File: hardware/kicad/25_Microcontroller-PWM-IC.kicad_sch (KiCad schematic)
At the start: 16 parts, among them U78 PCA9685PW,118

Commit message: starting erc check
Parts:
- C117, C118: footprint Capacitor_SMD:C_0603_1608Metric -> 5v rail sm-easyedapro:C0603
- R170, R171, R176, R177, R178, R179, R180: footprint Resistor_SMD:R_0603_1608Metric -> 5v rail sm-easyedapro:R0603
- R181, R182, R183, R184, R186, R188: footprint Resistor_SMD:R_0402_1005Metric -> 5v rail sm-easyedapro:R0402; LCSC Part Name 厚膜电阻 10kΩ ±1% 50mW -> 10kΩ ±1% 62.5mW 厚膜电阻; Manufacturer YAGEO(国巨) -> UNI-ROYAL(厚声); Manufacturer Part RC0201FR-0710KL -> 0402WGF1002TCE; Supplier Part C106225 -> C25744
- U78: footprint Package_SO:TSSOP-28_4.4x9.7mm_P0.65mm -> 5v rail sm-easyedapro:TSSOP-28_L9.7-W4.4-P0.65-LS6.4-TL

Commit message: added protection to servo pins
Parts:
- removed R170, R171, R176, R177, R178, R179, R180: 47Ω, 5v rail sm-easyedapro:R0603, symbol 5v rail sm-easyedapro:RS-03K47R0FT
- added U3201: EXB2HV102JV, JLCImport:EXB2HV102JV, symbol JLCImport:EXB2HV102JV
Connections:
- net OUT0: now also U3201.1
- net OUT1: now also U3201.2
- net OUT2: now also U3201.3
- net OUT3: now also U3201.4
- net OUT4: now also U3201.5
- net OUT5: now also U3201.6
- net OUT6: now also U3201.7
- net at U78.6 (LED0): now also U3201.16
- net at U78.10 (LED4): now also U3201.12
- net at U78.7 (LED1): now also U3201.15
- net at U78.8 (LED2): now also U3201.14
- net at U78.9 (LED3): now also U3201.13
- net at U78.12 (LED6): now also U3201.10
- net at U78.11 (LED5): now also U3201.11

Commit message: Update KiCad footprints and schematic placements
Convert and normalize multiple KiCad footprints and adjust schematic symbol placements. Upgraded EasyEDA and JLCImport footprints to modern pcbnew/footprint format (updated fp_line/pad primitives, uuids, embedded fonts/models), adjusted 3D model offsets, and expanded pad metadata. In schematics: moved EXB2HV102JV symbol position and added mirror Y, removed fields_autoplaced, set instance project path for U3201, and updated ServoConnectors port2 label to "sbus 3V". Also refreshed various PCB fp element UUIDs in svea_powerboard_rev3.kicad_pcb.
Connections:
- net OUT0: now also U3201.16; no longer U3201.1
- net OUT1: now also U3201.15; no longer U3201.2
- net OUT2: now also U3201.14; no longer U3201.3
- net OUT3: now also U3201.13; no longer U3201.4
- net OUT4: now also U3201.12; no longer U3201.5
- net OUT5: now also U3201.11; no longer U3201.6
- net OUT6: now also U3201.10; no longer U3201.7
- net at U78.12 (LED6): now also U3201.7; no longer U3201.10
- net at U78.11 (LED5): now also U3201.6; no longer U3201.11
- net at U78.10 (LED4): now also U3201.5; no longer U3201.12
- net at U78.9 (LED3): now also U3201.4; no longer U3201.13
- net at U78.8 (LED2): now also U3201.3; no longer U3201.14
- net at U78.7 (LED1): now also U3201.2; no longer U3201.15
- net at U78.6 (LED0): now also U3201.1; no longer U3201.16
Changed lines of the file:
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@@
 	(symbol
 		(lib_id "JLCImport:EXB2HV102JV")
-		(at 129.54 115.57 0)
+		(at 127 115.57 0)
+		(mirror y)
 		(unit 1)
 		(exclude_from_sim no)
@@
 		(on_board yes)
 		(dnp no)
-		(fields_autoplaced yes)
 		(property "Reference" "U3201"
 			(at 128.27 100.33 0)
@@
 		)
 		(property "Footprint" "JLCImport:EXB2HV102JV"
-			(at 129.54 115.57 0)
+			(at 127 115.57 0)
 			(effects
 				(font
@@
 		)
 		(property "Datasheet" "https://wmsc.lcsc.com/wmsc/upload/file/pdf/v2/lcsc/2011031536_PANASONIC-EXB2HV102JV_C713453.pdf"
-			(at 129.54 115.57 0)
+			(at 127 115.57 0)
 			(effects
 				(font
@@
 		)
 		(property "Description" "16 1kΩ 63mW 8 ±200ppm/℃ ±5% SMD-16P,3.8x1.6mm Resistor Networks, Arrays ROHS"
-			(at 129.54 115.57 0)
+			(at 127 115.57 0)
 			(effects
 				(font
@@
 		)
 		(property "LCSC" "C713453"
-			(at 129.54 115.57 0)
+			(at 127 115.57 0)
 			(effects
 				(font
@@
 		)
 		(property "Manufacturer" "PANASONIC"
-			(at 129.54 115.57 0)
+			(at 127 115.57 0)
 			(effects
 				(font
@@
 		)
 		(property "Manufacturer Part" "EXB2HV102JV"
-			(at 129.54 115.57 0)
+			(at 127 115.57 0)
 			(effects
 				(font
@@
 		)
 		(instances
-			(project ""
+			(project "svea_powerboard_rev3"
 				(path "/3f85abf4-0b95-4c4a-b7e9-06f59ca1ea3d/5c2e021f-c2d4-49e2-8c36-9a64f1f12001/8281c4bd-f2fa-451b-b37c-f7eda375ddce"
 					(reference "U3201")

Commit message: updating symbols to use kicad footprints where possible
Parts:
- C117, C118: footprint 5v rail sm-easyedapro:C0603 -> Capacitor_SMD:C_0603_1608Metric
- R181, R182, R183, R184, R186, R188: footprint 5v rail sm-easyedapro:R0402 -> Resistor_SMD:R_0402_1005Metric
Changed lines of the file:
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@@
 			)
 		)
-		(property "Footprint" "5v rail sm-easyedapro:R0402"
+		(property "Footprint" "Resistor_SMD:R_0402_1005Metric"
 			(at 130.81 72.39 0)
 			(effects
@@
 			)
 		)
-		(property "Footprint" "5v rail sm-easyedapro:R0402"
+		(property "Footprint" "Resistor_SMD:R_0402_1005Metric"
 			(at 196.85 107.95 0)
 			(effects
@@
 			)
 		)
-		(property "Footprint" "5v rail sm-easyedapro:C0603"
+		(property "Footprint" "Capacitor_SMD:C_0603_1608Metric"
 			(at 251.46 74.93 0)
 			(effects
@@
 			)
 		)
-		(property "Footprint" "5v rail sm-easyedapro:R0402"
+		(property "Footprint" "Resistor_SMD:R_0402_1005Metric"
 			(at 166.37 64.77 0)
 			(effects
@@
 			)
 		)
-		(property "Footprint" "5v rail sm-easyedapro:R0402"
+		(property "Footprint" "Resistor_SMD:R_0402_1005Metric"
 			(at 130.81 87.63 0)
 			(effects
@@
 			)
 		)
-		(property "Footprint" "5v rail sm-easyedapro:R0402"
+		(property "Footprint" "Resistor_SMD:R_0402_1005Metric"
 			(at 130.81 64.77 0)
 			(effects
@@
 			)
 		)
-		(property "Footprint" "5v rail sm-easyedapro:C0603"
+		(property "Footprint" "Capacitor_SMD:C_0603_1608Metric"
 			(at 236.22 74.93 0)
 			(effects
@@
 			)
 		)
-		(property "Footprint" "5v rail sm-easyedapro:R0402"
+		(property "Footprint" "Resistor_SMD:R_0402_1005Metric"
 			(at 130.81 80.01 0)
 			(effects

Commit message: updated more footprints
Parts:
- U78: footprint 5v rail sm-easyedapro:TSSOP-28_L9.7-W4.4-P0.65-LS6.4-TL -> Package_SO:TSSOP-28_4.4x9.7mm_P0.65mm
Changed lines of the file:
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@@
 			)
 		)
-		(property "Footprint" "5v rail sm-easyedapro:TSSOP-28_L9.7-W4.4-P0.65-LS6.4-TL"
+		(property "Footprint" "Package_SO:TSSOP-28_4.4x9.7mm_P0.65mm"
 			(at 171.45 111.76 0)
 			(effects

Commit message: various erc fixes
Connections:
- no-connect marks 0 -> 11
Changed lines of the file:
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@@
 		(color 0 0 0 0)
+	)
+	(no_connect
+		(at 184.15 115.57)
+	)
+	(no_connect
+		(at 184.15 118.11)
+	)
+	(no_connect
+		(at 184.15 110.49)
+	)
+	(no_connect
+		(at 184.15 123.19)
+	)
+	(no_connect
+		(at 184.15 128.27)
+	)
+	(no_connect
+		(at 184.15 125.73)
+	)
+	(no_connect
+		(at 120.65 125.73)
+	)
+	(no_connect
+		(at 184.15 120.65)
+	)
+	(no_connect
+		(at 135.89 125.73)
+	)
+	(no_connect
+		(at 184.15 113.03)
+	)
+	(no_connect
+		(at 158.75 125.73)
 	)
 	(wire

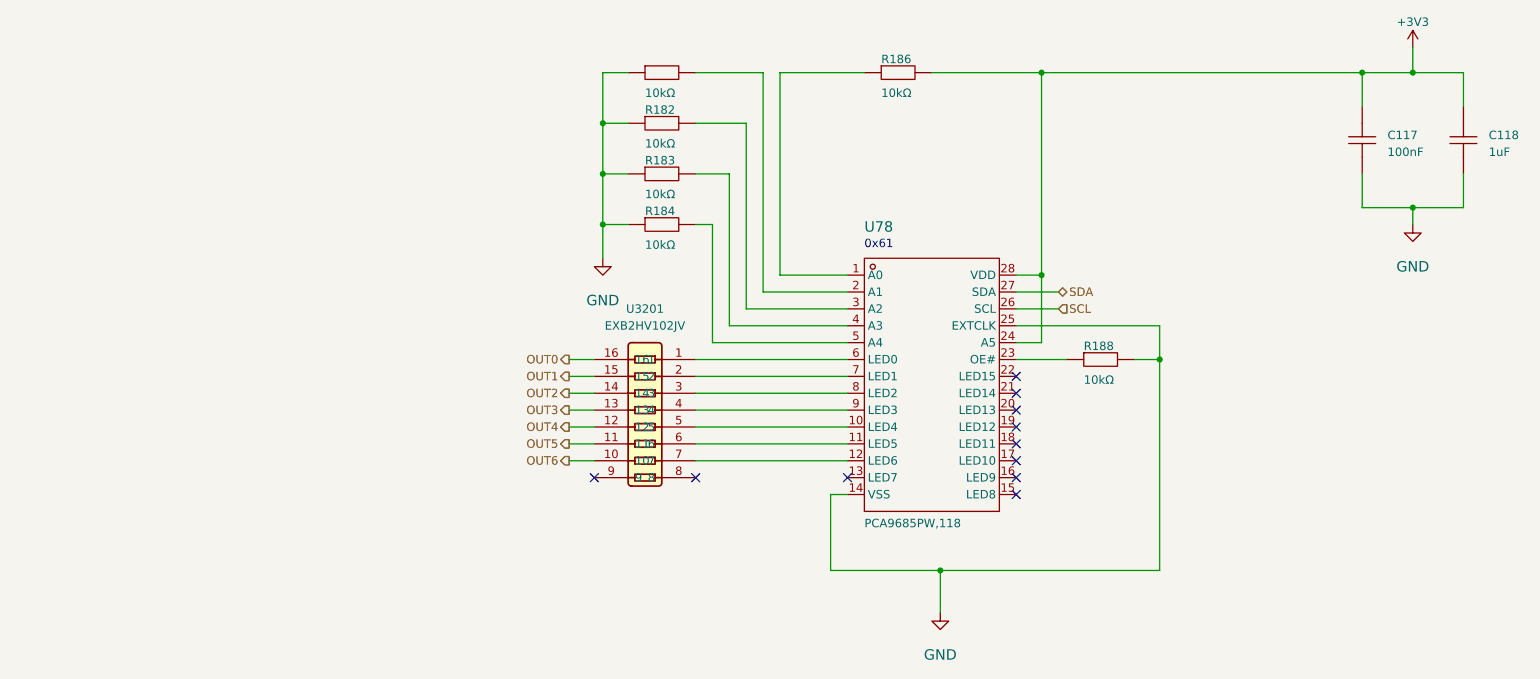
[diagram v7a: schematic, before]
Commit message: fixing inconsistencies in value convention
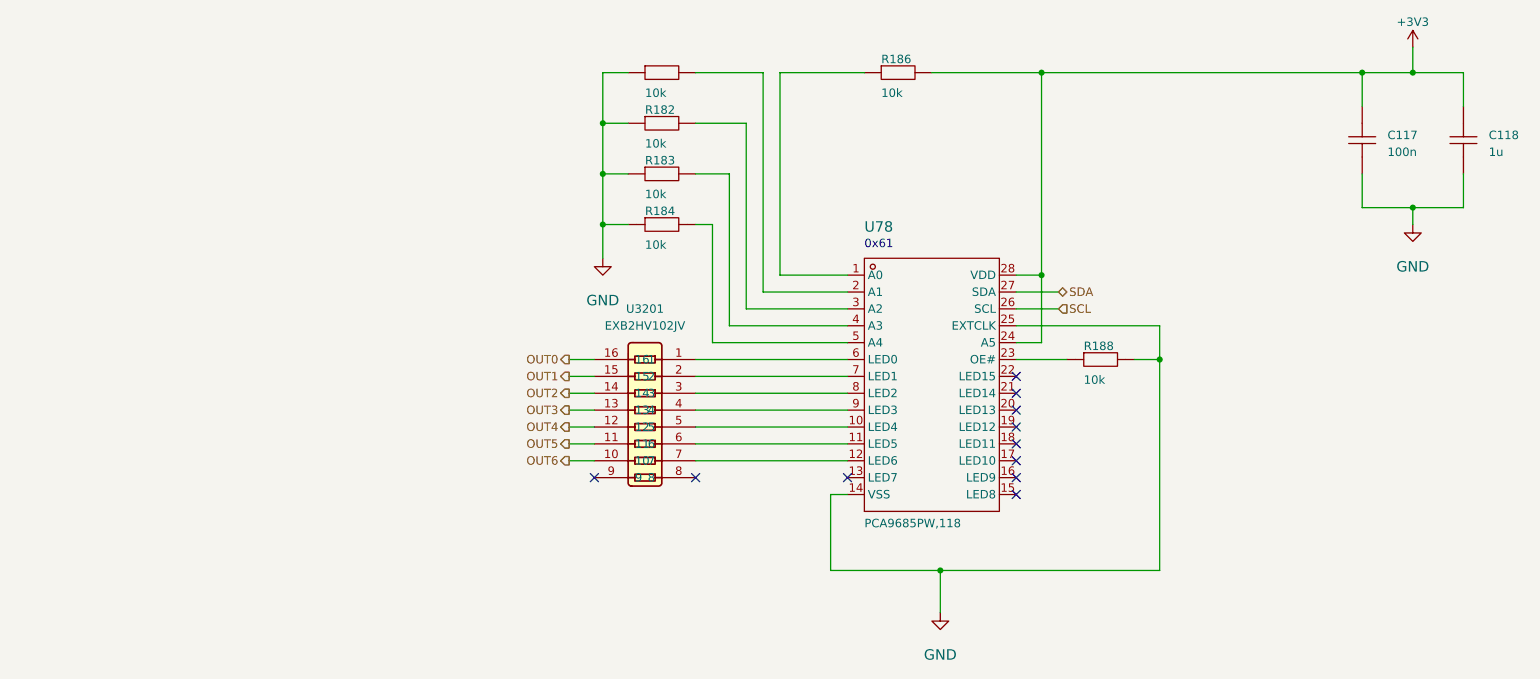
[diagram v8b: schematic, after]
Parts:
- C117: value 100nF -> 100n
- C118: value 1uF -> 1u
- R181, R182, R183, R184, R186, R188: value 10kΩ -> 10k
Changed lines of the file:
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@@
 			)
 		)
-		(property "Value" "10kΩ"
+		(property "Value" "10k"
 			(at 128.27 76.2 0)
 			(effects
@@
 			)
 		)
-		(property "Value" "10kΩ"
+		(property "Value" "10k"
 			(at 194.31 111.76 0)
 			(effects
@@
 			)
 		)
-		(property "Value" "1uF"
+		(property "Value" "1u"
 			(at 255.27 77.47 90)
 			(effects
@@
 			)
 		)
-		(property "Value" "10kΩ"
+		(property "Value" "10k"
 			(at 163.83 68.58 0)
 			(effects
@@
 			)
 		)
-		(property "Value" "10kΩ"
+		(property "Value" "10k"
 			(at 128.27 91.44 0)
 			(effects
@@
 			)
 		)
-		(property "Value" "10kΩ"
+		(property "Value" "10k"
 			(at 128.27 68.58 0)
 			(effects
@@
 			)
 		)
-		(property "Value" "100nF"
+		(property "Value" "100n"
 			(at 240.03 77.47 90)
 			(effects
@@
 			)
 		)
-		(property "Value" "10kΩ"
+		(property "Value" "10k"
 			(at 128.27 83.82 0)
 			(effects
